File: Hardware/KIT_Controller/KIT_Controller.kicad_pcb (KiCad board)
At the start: 2 copper layers, 115.8 x 99.2 mm, 49 parts, among them J201 USB_B, J202 USB_BOOT, U101 Nokia_5110_LCD, U201 TCA9554DB, U202 W25Q128JVS, U203 NCP1117-3.3_SOT223, U204 HDSP-7401, U205 RP2040, Y201 Crystal

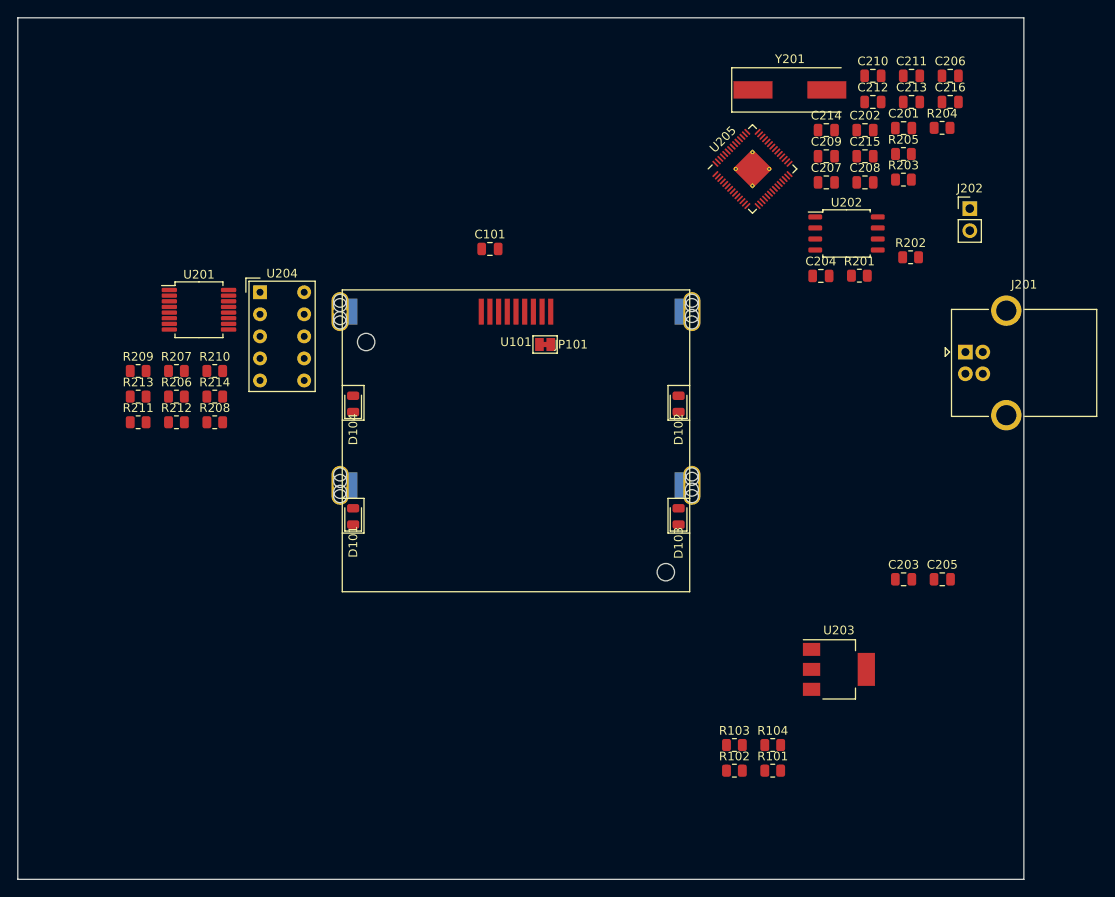
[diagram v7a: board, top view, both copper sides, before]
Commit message: Add short range modem
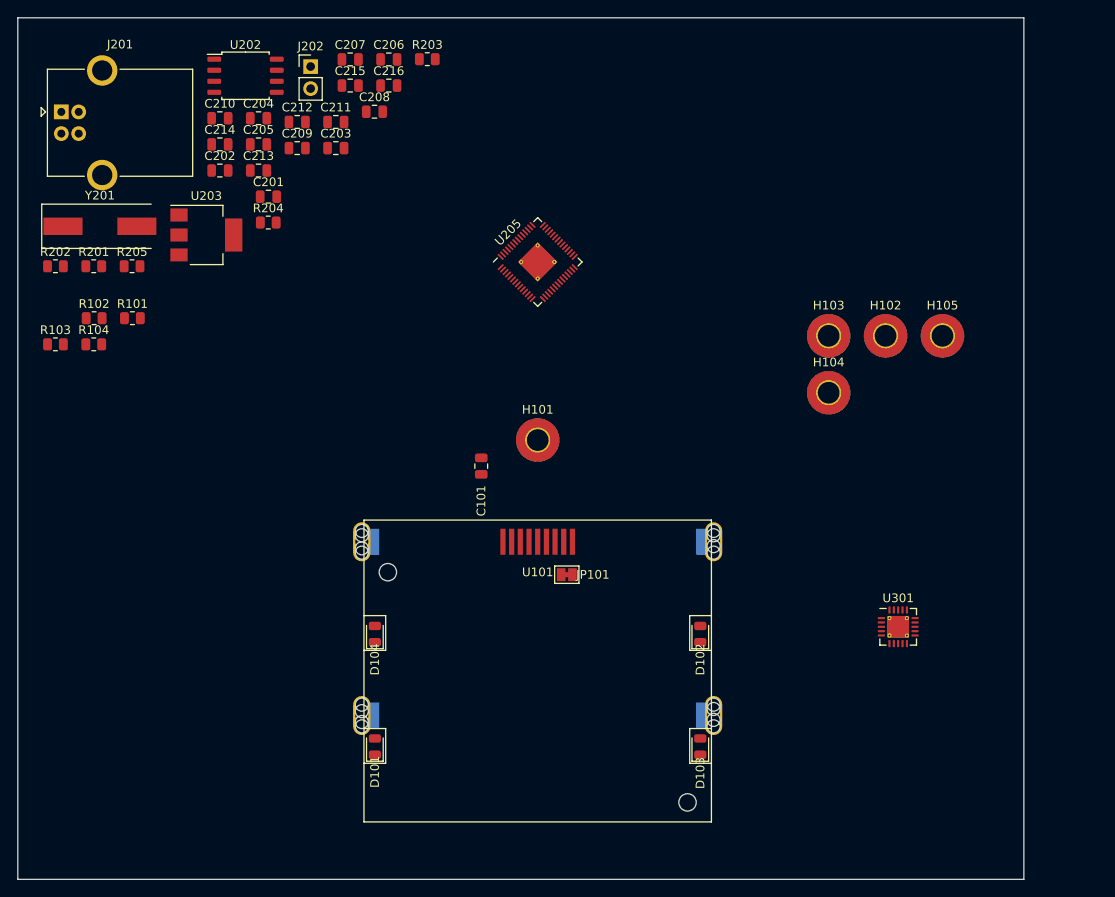
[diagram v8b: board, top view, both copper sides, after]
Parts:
- removed R206: 10k, Resistor_SMD:R_0805_2012Metric
- removed R207, R208, R209, R210, R211, R212, R213, R214: 240, Resistor_SMD:R_0805_2012Metric
- removed U201: TCA9554DB, Package_SO:SSOP-16_5.3x6.2mm_P0.65mm
- removed U204: HDSP-7401, Display_7Segment:HDSP-7401
- added H101: MountingHole_Pad, MountingHole:MountingHole_2.5mm_Pad_TopBottom, F.Cu at (148.5, 105.0)
- added H102: MountingHole_Pad, MountingHole:MountingHole_2.5mm_Pad_TopBottom, F.Cu at (188.6, 93.0)
- added H103: MountingHole_Pad, MountingHole:MountingHole_2.5mm_Pad_TopBottom, F.Cu at (182.0, 93.0)
- added H104: MountingHole_Pad, MountingHole:MountingHole_2.5mm_Pad_TopBottom, F.Cu at (182.0, 99.5)
- added H105: MountingHole_Pad, MountingHole:MountingHole_2.5mm_Pad_TopBottom, F.Cu at (195.1, 93.0)
- added U301: CC1101, Package_DFN_QFN:QFN-20-1EP_4x4mm_P0.5mm_EP2.5x2.5mm_ThermalVias, F.Cu at (190.0, 126.5)
- moved J201 107.7 mm to (93.7, 67.2)
- moved R202 98.5 mm to (93.0, 85.0)
- moved C205 93.3 mm to (116.4, 71.0)
- moved R103 90.8 mm to (93.0, 94.0)
- moved R104 90.8 mm to (97.4, 94.0)
- moved R101 90.3 mm to (101.8, 91.0)
- moved R102 90.3 mm to (97.4, 91.0)
- moved R205 89.7 mm to (101.8, 85.0)
- moved U203 88.3 mm to (110.3, 81.4)
- moved R201 88.1 mm to (97.4, 85.0)
- moved C203 82.1 mm to (125.3, 71.4)
- moved Y201 81.0 mm to (98.1, 80.4)
- moved R204 78.3 mm to (117.5, 80.0)
- moved J202 77.6 mm to (122.4, 62.0)
- moved C213 75.6 mm to (116.4, 74.0)
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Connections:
- U205 pad 27: unconnected-(U205-Pad27) -> /MCU/MISO
- U205 pad 29: unconnected-(U205-Pad29) -> /MCU/SCK
- U205 pad 30: unconnected-(U205-Pad30) -> /MCU/MOSI
